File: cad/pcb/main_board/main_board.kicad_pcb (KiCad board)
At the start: 4 copper layers, 71 parts, among them J1 USB_B_Micro, SW1 SW_DIP_x02, SW2 SW_DIP_x01, U1 STM32F401R_B-C_Tx, U2 TLV75533PDQNR

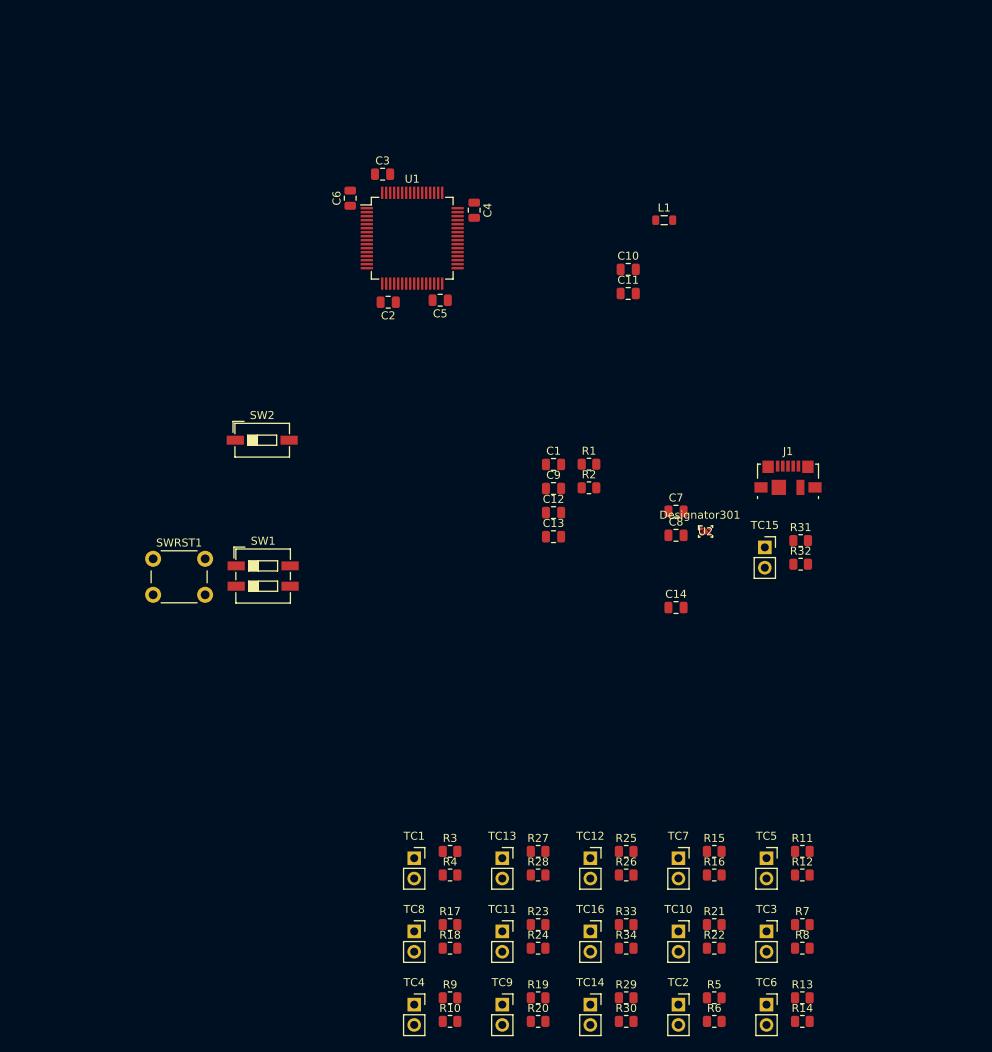
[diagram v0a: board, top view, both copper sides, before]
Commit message: Upgrading to kicad 8.0, adding aisler drc
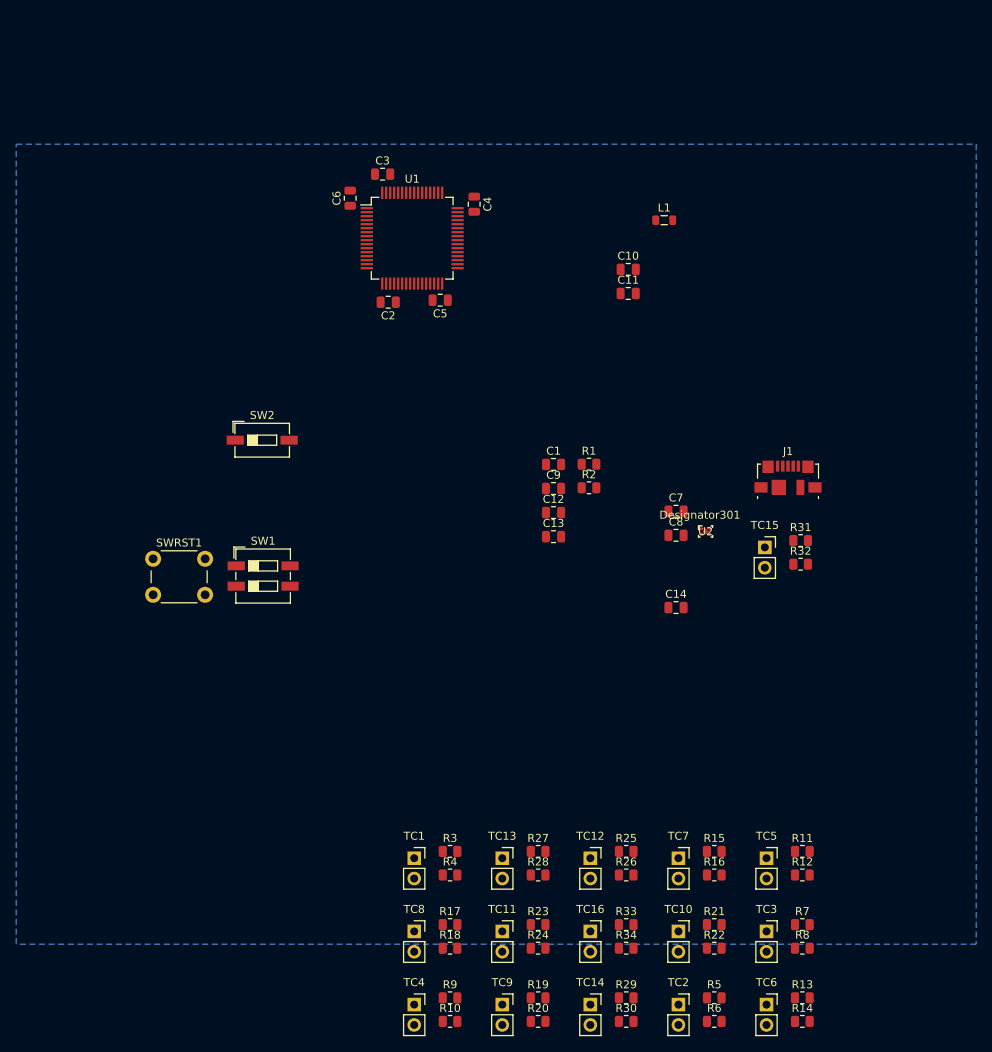
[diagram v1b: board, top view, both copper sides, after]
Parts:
- moved C4 0.75 mm to (117.2, 47.5)
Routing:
- added copper zone on B.Cu, net VSS
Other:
- copper layers 4 -> 2

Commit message: First Layout of Voltage Regulator, Status LED note, add pulldown resistor for Voltage Regulator Enable
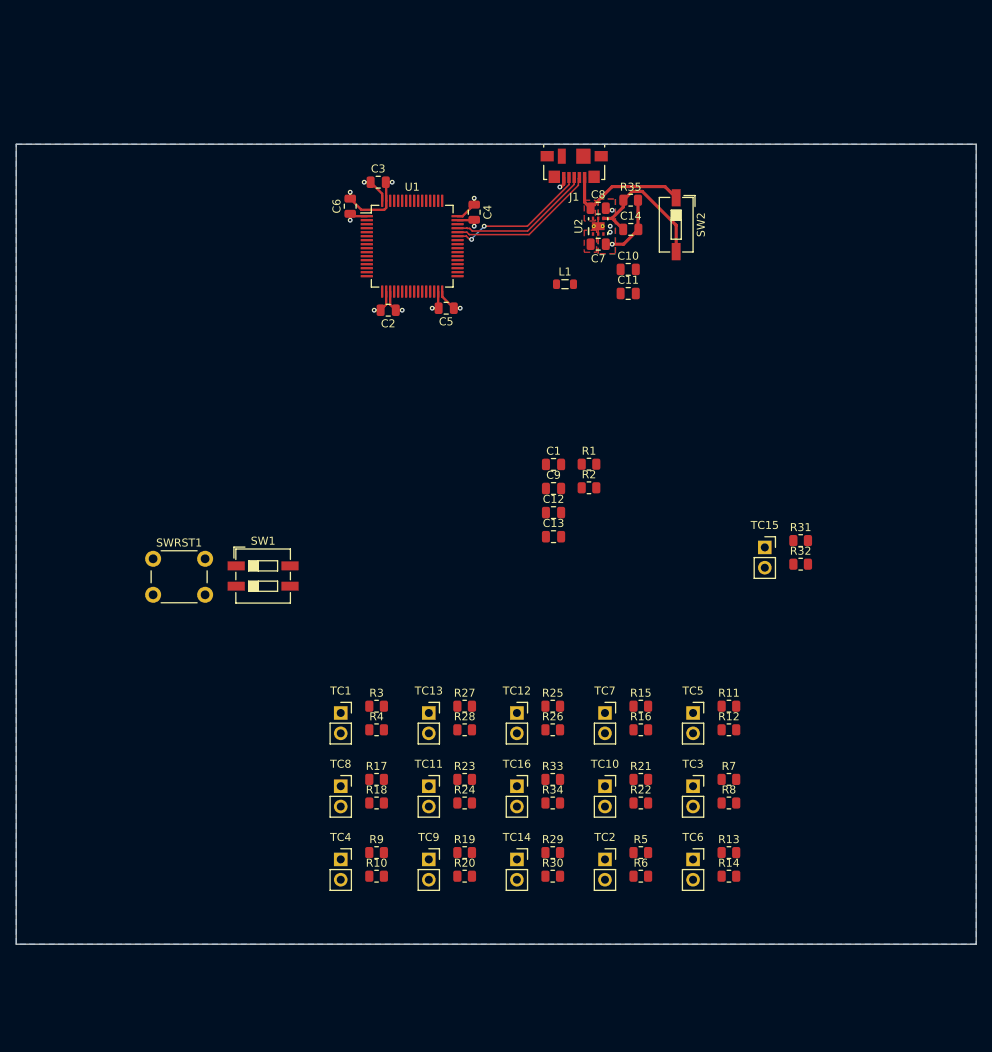
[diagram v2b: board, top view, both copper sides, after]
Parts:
- added R35: 10k, Resistor_SMD:R_0805_2012Metric, F.Cu at (136.8, 47.0)
- U2: value TLV75533PDQNR -> TLV75533PDRVR; footprint local:DQN0004A -> local:DRV0006A
- moved SW2 58.3 mm to (142.5, 50.1), turned to -90 degrees
- moved C14 47.6 mm to (136.8, 50.6)
- moved J1 47.3 mm to (129.8, 42.7), turned to 180 degrees
- moved C8 42.0 mm to (132.8, 48.0), turned to 180 degrees
- moved U2 40.5 mm to (132.8, 50.2), turned to 90 degrees
- moved C7 34.8 mm to (132.8, 52.5)
- moved R10 20.3 mm to (105.0, 131.5)
- moved R11 20.3 mm to (149.1, 110.2)
- moved R14 20.3 mm to (149.1, 131.5)
- moved R15 20.3 mm to (138.1, 110.2)
- moved R17 20.3 mm to (105.0, 119.4)
- moved R18 20.3 mm to (105.0, 122.3)
- moved R21 20.3 mm to (138.1, 119.4)
- moved R22 20.3 mm to (138.1, 122.3)
- moved R25 20.3 mm to (127.1, 110.2)
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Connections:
- U1 pad 12: VSSA -> VSS
- U2 pad 2: VSS -> unconnected-(U2-NC-Pad2)
- U2 pad 3: Net-(U2-EN) -> VSS
- U2 pad 4: VBUS -> Net-(U2-EN)
- U2 pad 5: VSS -> unconnected-(U2-NC-Pad5)
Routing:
- net VSS: track 0.00 -> 30.0 mm, vias 0 -> 10
- net /MCU/USB_D-: track 0.00 -> 18.8 mm
- net Net-(U2-EN): track 0.00 -> 18.1 mm
- net /MCU/USB_D+: track 0.00 -> 18.0 mm
- net /MCU/USB_ID: track 0.00 -> 17.9 mm, vias 0 -> 2
- net VDD: track 0.00 -> 17.1 mm, vias 0 -> 5
- net VBUS: track 0.00 -> 17.0 mm
- added copper zone on F.Cu, net VBUS
- added copper zone on F.Cu, net VDD
- added copper zone on F.Cu, net VSS
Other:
- board outline added: 120 x 100 mm

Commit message: Tighter Layout for USB Micro and Power Delivery. Worse design for ADC routing on left side of MCU.
Revise revise revise
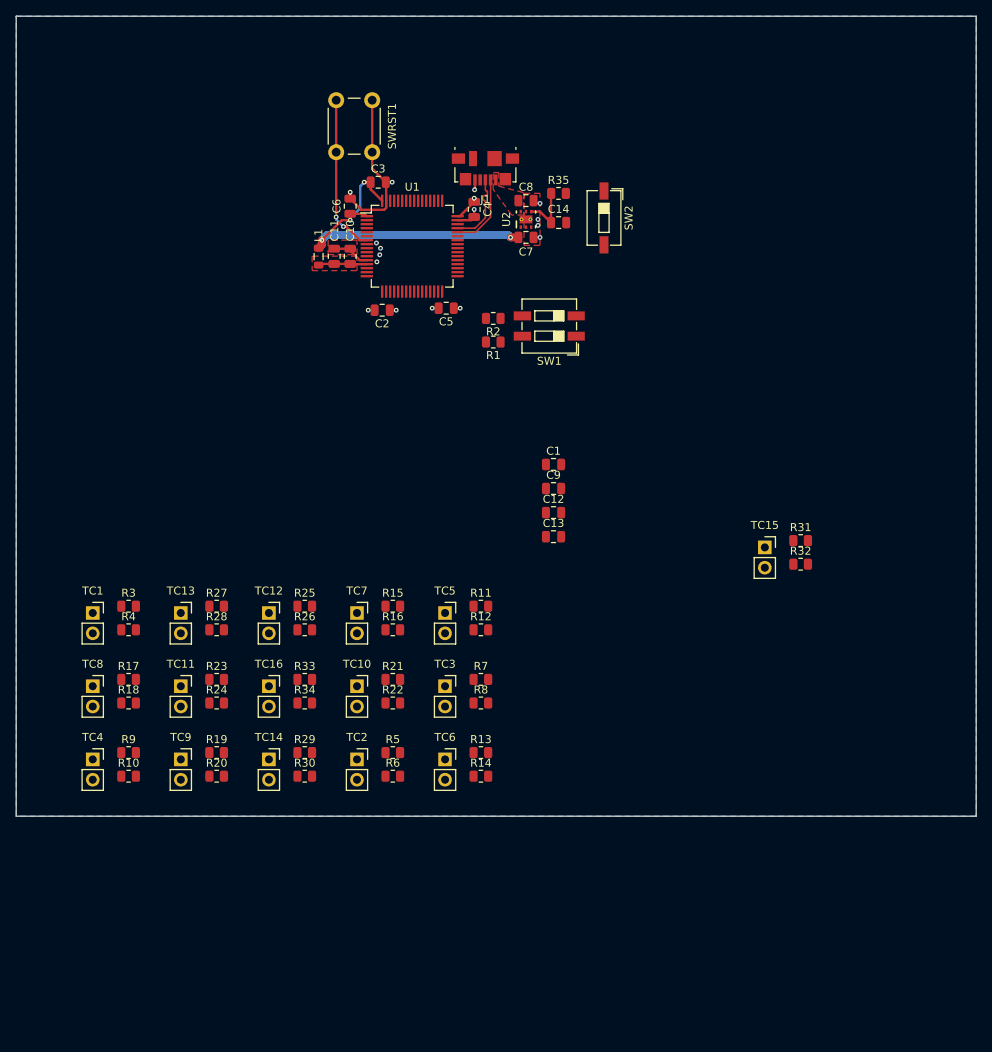
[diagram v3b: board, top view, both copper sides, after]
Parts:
- moved SWRST1 55.7 mm to (100.0, 41.0), turned to 90 degrees
- moved SW1 47.5 mm to (126.6, 62.7), turned to 180 degrees
- moved C11 37.0 mm to (99.8, 54.0), turned to 90 degrees
- moved C10 34.8 mm to (101.8, 54.0), turned to 90 degrees
- moved R13 33.4 mm to (118.1, 116.0)
- moved R19 33.4 mm to (85.1, 116.0)
- moved R29 33.4 mm to (96.1, 116.0)
- moved R9 33.4 mm to (74.0, 116.0)
- moved R10 33.4 mm to (74.0, 119.0)
- moved R11 33.4 mm to (118.1, 97.8)
- moved R12 33.4 mm to (118.1, 100.7)
- moved R14 33.4 mm to (118.1, 119.0)
- moved R17 33.4 mm to (74.0, 106.9)
- moved R18 33.4 mm to (74.0, 109.8)
- moved R20 33.4 mm to (85.1, 119.0)
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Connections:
- U2 pad 2: unconnected-(U2-NC-Pad2) -> VSS
- U2 pad 5: unconnected-(U2-NC-Pad5) -> VSS
- U2 pad V: (no net) -> VSS
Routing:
- net VDD: track 17.1 -> 45.5 mm, vias 5 -> 7
- net Net-(U1-NRST): track 0.00 -> 19.8 mm, vias 0 -> 2
- net /MCU/USB_ID: track 17.9 -> 0.00 mm, vias 2 -> 0
- net VBUS: track 17.0 -> 0.00 mm
- net Net-(U2-EN): track 18.1 -> 6.70 mm
- net /MCU/USB_D-: track 18.8 -> 9.57 mm
- net /MCU/USB_D+: track 18.0 -> 9.53 mm
- net VDDA: track 0.00 -> 6.10 mm
- net /MCU/ADC_IN13: vias 0 -> 1
- net /MCU/ADC_IN12: vias 0 -> 1
- net /MCU/ADC_IN11: vias 0 -> 1
- net /MCU/ADC_IN10: vias 0 -> 1
- added copper zone on F.Cu, net VDDA
- removed copper zone on F.Cu, net VDD
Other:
- board text added: "This is not good, the ADC IN get the noisiest parts Of the pcb"

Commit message: Some more routing
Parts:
- moved R1 6.97 mm to (119.3, 57.8)
- moved R2 6.55 mm to (119.6, 55.2)
- moved SW1 6.25 mm to (126.2, 56.5)
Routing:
- net BOOT0: track 0.00 -> 17.1 mm
- net VBUS: track 0.00 -> 11.8 mm
- net BOOT1: track 0.00 -> 9.40 mm, vias 0 -> 2
- net Net-(U2-EN): track 6.70 -> 14.5 mm
- net VSS: track 30.2 -> 36.8 mm
- net VDD: track 45.5 -> 49.0 mm
- net Net-(R1-Pad1): track 0.00 -> 2.62 mm
- net Net-(R2-Pad1): track 0.00 -> 2.32 mm
- added copper zone on F.Cu, net VDD
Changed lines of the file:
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@@
 	(footprint "Button_Switch_SMD:SW_DIP_SPSTx02_Slide_6.7x6.64mm_W6.73mm_P2.54mm_LowProfile_JPin"
 		(layer "F.Cu")
-		(at 126.635 62.73 180)
+		(at 126.2 56.5 180)
 		(descr "SMD 2x-dip-switch SPST , Slide, row spacing 6.73 mm (264 mils), body size 6.7x6.64mm (see e.g. https://www.ctscorp.com/wp-content/uploads/219.pdf), SMD, LowProfile, JPin")
 		(tags "SMD DIP Switch SPST Slide 6.73mm 264mil SMD LowProfile JPin")
@@
 	(footprint "Resistor_SMD:R_0805_2012Metric"
 		(layer "F.Cu")
-		(at 119.635 64.73 180)
+		(at 119.3 57.77 180)
 		(descr "Resistor SMD 0805 (2012 Metric), square (rectangular) end terminal, IPC_7351 nominal, (Body size source: IPC-SM-782 page 72, https://www.pcb-3d.com/wordpress/wp-content/uploads/ipc-sm-782a_amendment_1_and_2.pdf), generated with kicad-footprint-generator")
 		(tags "resistor")
@@
 	(footprint "Resistor_SMD:R_0805_2012Metric"
 		(layer "F.Cu")
-		(at 119.635 61.78 180)
+		(at 119.6 55.23 180)
 		(descr "Resistor SMD 0805 (2012 Metric), square (rectangular) end terminal, IPC_7351 nominal, (Body size source: IPC-SM-782 page 72, https://www.pcb-3d.com/wordpress/wp-content/uploads/ipc-sm-782a_amendment_1_and_2.pdf), generated with kicad-footprint-generator")
 		(tags "resistor")
@@
 	)
 	(segment
+		(start 128.7 46.15)
+		(end 128.7 49.75)
+		(width 0.3)
+		(layer "F.Cu")
+		(net 2)
+	)
+	(segment
+		(start 112.75 60.45)
+		(end 112.8 60.5)
+		(width 0.3)
+		(layer "F.Cu")
+		(net 2)
+	)
+	(segment
 		(start 115.175 49.5)
 		(end 116.85 49.5)
@@
 	)
 	(segment
+		(start 112.8 60.5)
+		(end 112 60.5)
+		(width 0.3)
+		(layer "F.Cu")
+		(net 2)
+	)
+	(segment
 		(start 102.94688 54.5)
 		(end 101.75 53.30312)
@@
 		(net 2)
 	)
+	(segment
+		(start 128.7 49.75)
+		(end 128.75 49.8)
+		(width 0.3)
+		(layer "F.Cu")
+		(net 2)
+	)
+	(segment
+		(start 112.75 58.425)
+		(end 112.75 60.45)
+		(width 0.3)
+		(layer "F.Cu")
+		(net 2)
+	)
 	(via
 		(at 112 60.5)
@@
 	)
 	(segment
+		(start 113.25 58.425)
+		(end 113.25 59.05)
+		(width 0.3)
+		(layer "F.Cu")
+		(net 3)
+	)
+	(segment
 		(start 101.75 49.5)
 		(end 100.7 49.5)
@@
 	)
 	(segment
+		(start 114.7 60.5)
+		(end 115.5 60.5)
+		(width 0.3)
+		(layer "F.Cu")
+		(net 3)
+	)
+	(segment
 		(start 103.5 44.75)
 		(end 103.75 44.75)
@@
 	)
 	(segment
+		(start 113.25 59.05)
+		(end 114.7 60.5)
+		(width 0.3)
+		(layer "F.Cu")
+		(net 3)
+	)
+	(segment
 		(start 115.175 49)
 		(end 115.45 49)
@@
 	)
 	(segment
+		(start 124.725 45.1)
+		(end 122.775 47.05)
+		(width 0.3)
+		(layer "F.Cu")
+		(net 4)
+	)
+	(segment
+		(start 132.725 45.1)
+		(end 124.725 45.1)
+		(width 0.3)
+		(layer "F.Cu")
+		(net 4)
+	)
+	(segment
+		(start 133.475 45.85)
+		(end 132.725 45.1)
+		(width 0.3)
+		(layer "F.Cu")
+		(net 4)
+	)
+	(segment
 		(start 100.9 50.3)
 		(end 101.24688 50.3)
@@
 	)
 	(segment
+		(start 126.85 49.8)
+		(end 129.63 52.58)
+		(width 0.3)
+		(layer "F.Cu")
+		(net 9)
+	)
+	(segment
 		(start 125.475001 48.425001)
 		(end 124.374999 48.425001)
@@
 	)
 	(segment
+		(start 129.63 52.58)
+		(end 133.475 52.58)
+		(width 0.3)
+		(layer "F.Cu")
+		(net 9)
+	)
+	(segment
 		(start 115.175 51)
 		(end 117.42543 51)
@@
 		(net 11)
 	)
+	(segment
+		(start 122.835 57.77)
+		(end 120.2125 57.77)
+		(width 0.3)
+		(layer "F.Cu")
+		(net 14)
+	)
+	(segment
+		(start 115.146879 57.849999)
+		(end 107.75 50.45312)
+		(width 0.3)
+		(layer "F.Cu")
+		(net 15)
+	)
+	(segment
+		(start 118.3875 57.77)
+		(end 118.307501 57.849999)
+		(width 0.3)
+		(layer "F.Cu")
+		(net 15)
+	)
+	(segment
+		(start 118.307501 57.849999)
+		(end 115.146879 57.849999)
+		(width 0.3)
+		(layer "F.Cu")
+		(net 15)
+	)
+	(segment
+		(start 107.75 50.45312)
+		(end 107.75 47.075)
+		(width 0.3)
+		(layer "F.Cu")
+		(net 15)
+	)
+	(segment
+		(start 122.835 55.23)
+		(end 120.5125 55.23)
+		(width 0.3)
+		(layer "F.Cu")
+		(net 16)
+	)
+	(segment
+		(start 113.3 57)
+		(end 111.79688 57)
+		(width 0.3)
+		(layer "F.Cu")
+		(net 17)
+	)
+	(segment
+		(start 118.6875 55.23)
+		(end 116.767501 57.149999)
+		(width 0.3)
+		(layer "F.Cu")
+		(net 17)
+	)
+	(segment
+		(start 116.767501 57.149999)
+		(end 115.4 57.149999)
+		(width 0.3)
+		(layer "F.Cu")
+		(net 17)
+	)
+	(segment
+		(start 111.25 57.54688)
+		(end 111.25 58.425)
+		(width 0.3)
+		(layer "F.Cu")
+		(net 17)
+	)
+	(segment
+		(start 111.79688 57)
+		(end 111.25 57.54688)
+		(width 0.3)
+		(layer "F.Cu")
+		(net 17)
+	)
+	(via
+		(at 113.3 57)
+		(size 0.6)
+		(drill 0.3)
+		(layers "F.Cu" "B.Cu")
+		(net 17)
+	)
+	(via
+		(at 115.4 57.149999)
+		(size 0.6)
+		(drill 0.3)
+		(layers "F.Cu" "B.Cu")
+		(net 17)
+	)
+	(segment
+		(start 115.4 57.149999)
+		(end 113.449999 57.149999)
+		(width 0.3)
+		(layer "B.Cu")
+		(net 17)
+	)
+	(segment
+		(start 113.449999 57.149999)
+		(end 113.3 57)
+		(width 0.3)
+		(layer "B.Cu")
+		(net 17)
+	)
 	(via
 		(at 105.031093 52.35)
@@
 	)
 	(zone
+		(net 3)
+		(net_name "VDD")
+		(layer "F.Cu")
+		(hatch edge 0.5)
+		(priority 4)
+		(connect_pads yes
+			(clearance 0.2)
+		)
+		(min_thickness 0.25)
+		(filled_areas_thickness no)
+		(fill yes
+			(thermal_gap 0.5)
+			(thermal_bridge_width 0.5)
+		)
+		(polygon
+			(pts
+				(xy 123.3 52.6) (xy 122 52.6) (xy 122 50) (xy 123.3 50)
+			)
+		)
+	)
+	(zone
 		(net 2)
 		(net_name "VSS")
@@
 			"2e4d690f-8446-41b5-b371-9c3c4c0bae19" "300f9093-da85-4912-a97a-4bbafb84713f"
 			"516af612-af63-4a49-aa45-5a57a48347b8" "5fb28761-f060-49b6-b95d-febaa13e213f"
-			"7e9ee241-cd4c-4b96-a62f-a67ce0e80392" "8bb36541-e01e-46be-bd12-be1804cd2843"
-			"8dc58c63-91fd-41f9-a451-21f15ff8f9d8" "98290dd6-9ee5-429a-8aca-7cb5bd7fa22c"
-			"9b1a8647-5208-4568-b195-c077c0df889c" "a0c95c98-05c6-4077-90ab-d4987b03f9ea"
-			"a20b145b-277d-416b-b9c5-f2b64d614613" "d4654a90-56dd-404b-899a-cc2d2dfbfd15"
-			"fcbff041-94b5-46f3-b584-6bb1db9daf7d"
+			"7996cb4c-d943-4b03-8d73-7ce1064106c1" "7e9ee241-cd4c-4b96-a62f-a67ce0e80392"
+			"8bb36541-e01e-46be-bd12-be1804cd2843" "8dc58c63-91fd-41f9-a451-21f15ff8f9d8"
+			"98290dd6-9ee5-429a-8aca-7cb5bd7fa22c" "9b1a8647-5208-4568-b195-c077c0df889c"
+			"a0c95c98-05c6-4077-90ab-d4987b03f9ea" "a20b145b-277d-416b-b9c5-f2b64d614613"
+			"d4654a90-56dd-404b-899a-cc2d2dfbfd15" "fcbff041-94b5-46f3-b584-6bb1db9daf7d"
 		)
 	)
